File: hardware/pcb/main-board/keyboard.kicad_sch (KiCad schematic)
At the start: 24 parts, among them J201 KB Pico Test Points, U201 KB Pico, U202 Unused 555

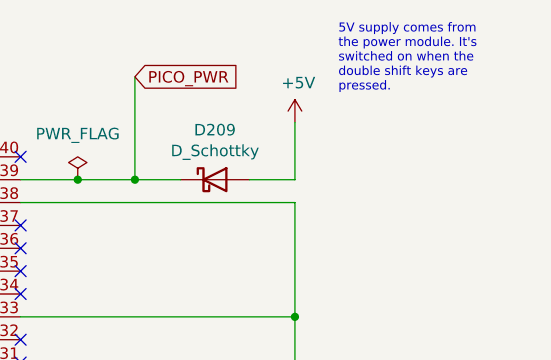
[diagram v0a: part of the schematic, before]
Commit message: start next board iteration, add latch and pico power bits
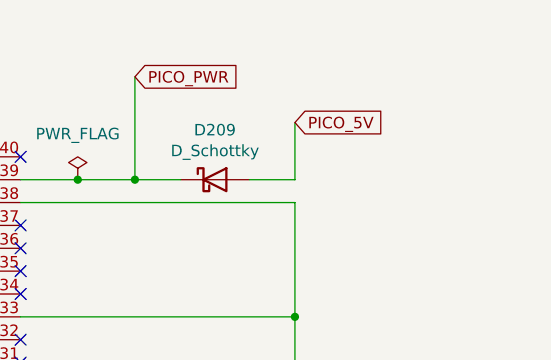
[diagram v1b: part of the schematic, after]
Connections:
- net +5V renamed PICO_5V
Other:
- note removed: "5V supply comes from the power module. It's switched on when the double shift keys are pressed."
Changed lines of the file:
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@@
 	(title_block
 		(title "Z88R - Z88 Recreated")
-		(date "2024-08-23")
-		(rev "20240823")
+		(date "2025-12-19")
+		(rev "20251219WIP")
 		(company "Fountain and Menadue")
 	)
@@
 		)
 	)
-	(text "5V supply comes from\nthe power module. It's\nswitched on when the\ndouble shift keys are\npressed."
-		(exclude_from_sim no)
-		(at 258.826 19.558 0)
-		(effects
-			(font
-				(size 1 1)
-			)
-			(justify left)
-		)
-	)
 	(text "Footprint for a 555, which was originally planned\nto wake the keyboard Pico every 10ms or so. The\nidea was dropped, but it might still be useful.\nNot sure where the 555's power will come from\nthough - the cell battery, like the RTC probably,\nbut it depends how we use it."
 		(exclude_from_sim no)
@@
 		)
 	)
+	(global_label "PICO_5V"
+		(shape input)
+		(at 254 26.67 0)
+		(fields_autoplaced yes)
+		(effects
+			(font
+				(size 1.27 1.27)
+			)
+			(justify left)
+		)
+		(property "Intersheetrefs" "${INTERSHEET_REFS}"
+			(at 264.072 26.67 0)
+			(effects
+				(font
+					(size 1.27 1.27)
+				)
+				(justify left)
+				(hide yes)
+			)
+		)
+	)
 	(global_label "KB_A14"
 		(shape input)
@@
 		(shape output)
 		(at 227.33 63.5 0)
-		(fields_autoplaced yes)
 		(effects
 			(font
@@
 		(shape output)
 		(at 227.33 71.12 0)
-		(fields_autoplaced yes)
 		(effects
 			(font
@@
 					(unit 1)
 				)
-			)
-		)
-	)
-	(symbol
-		(lib_id "power:+5V")
-		(at 254 26.67 0)
-		(unit 1)
-		(exclude_from_sim no)
-		(in_bom yes)
-		(on_board yes)
-		(dnp no)
-		(property "Reference" "#PWR0202"
-			(at 254 30.48 0)
-			(effects
-				(font
-					(size 1.27 1.27)
-				)
-				(hide yes)
-			)
-		)
-		(property "Value" "+5V"
-			(at 254.381 22.2758 0)
-			(effects
-				(font
-					(size 1.27 1.27)
-				)
-			)
-		)
-		(property "Footprint" ""
-			(at 254 26.67 0)
-			(effects
-				(font
-					(size 1.27 1.27)
-				)
-				(hide yes)
-			)
-		)
-		(property "Datasheet" ""
-			(at 254 26.67 0)
-			(effects
-				(font
-					(size 1.27 1.27)
-				)
-				(hide yes)
-			)
-		)
-		(property "Description" "Power symbol creates a global label with name \"+5V\""
-			(at 254 26.67 0)
-			(effects
-				(font
-					(size 1.27 1.27)
-				)
-				(hide yes)
-			)
-		)
-		(pin "1"
-		)
-		(instances
-			(project "z88_new"
-				(path "/fdce8012-5f35-4f58-8abb-80214b4af8fe/611ade0a-1c77-478f-8f5a-a9824ea3de3f"
-					(reference "#PWR0202")
-					(unit 1)
-				)

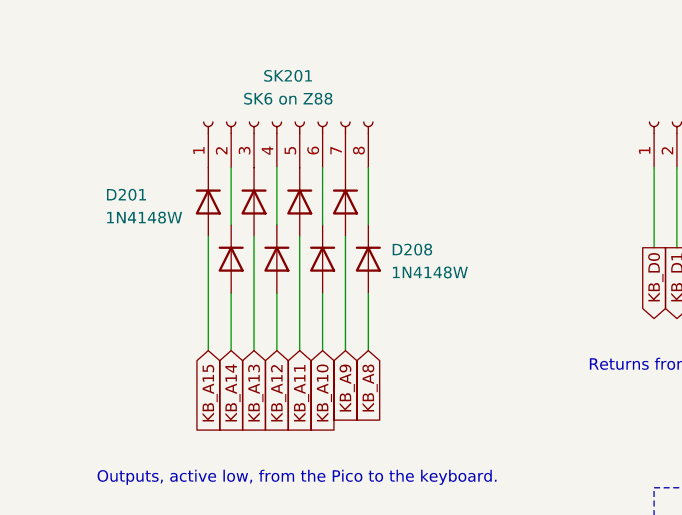
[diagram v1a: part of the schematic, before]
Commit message: turn the KB diodes round, oops
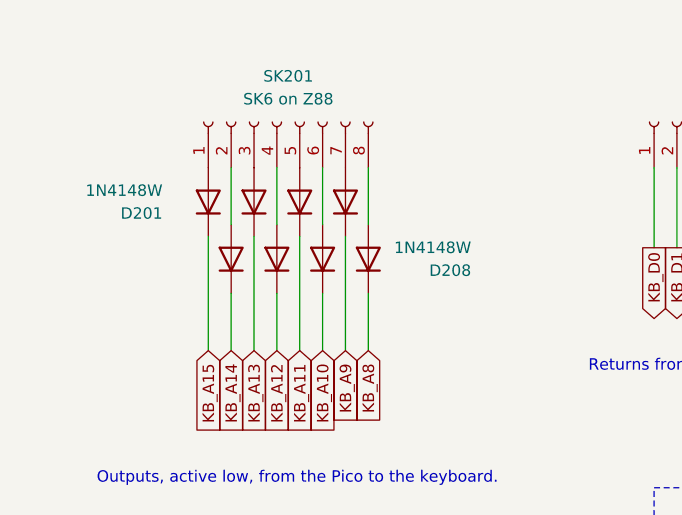
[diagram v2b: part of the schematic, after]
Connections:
- net KB_A10: now also D206.1 (K); no longer D206.2 (A)
- net KB_A11: now also D205.1 (K); no longer D205.2 (A)
- net KB_A12: now also D204.1 (K); no longer D204.2 (A)
- net KB_A13: now also D203.1 (K); no longer D203.2 (A)
- net KB_A14: now also D202.1 (K); no longer D202.2 (A)
- net KB_A15: now also D201.1 (K); no longer D201.2 (A)
- net KB_A8: now also D208.1 (K); no longer D208.2 (A)
- net KB_A9: now also D207.1 (K); no longer D207.2 (A)
- net at SK201.1 (Pin_1): now also D201.2 (A); no longer D201.1 (K)
- net at SK201.2 (Pin_2): now also D202.2 (A); no longer D202.1 (K)
- net at SK201.3 (Pin_3): now also D203.2 (A); no longer D203.1 (K)
- net at SK201.4 (Pin_4): now also D204.2 (A); no longer D204.1 (K)
- net at SK201.5 (Pin_5): now also D205.2 (A); no longer D205.1 (K)
- net at SK201.6 (Pin_6): now also D206.2 (A); no longer D206.1 (K)
- net at SK201.7 (Pin_7): now also D207.2 (A); no longer D207.1 (K)
- net at SK201.8 (Pin_8): now also D208.2 (A); no longer D208.1 (K)
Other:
- moved on the sheet: D201, D208
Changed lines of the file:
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@@
 	(symbol
 		(lib_id "Diode:1N4148W")
-		(at 38.1 40.64 270)
+		(at 38.1 40.64 90)
 		(unit 1)
 		(exclude_from_sim no)
@@
 		(dnp no)
 		(property "Reference" "D203"
-			(at 26.67 39.878 90)
+			(at 49.53 41.402 90)
 			(effects
 				(font
@@
 		)
 		(property "Value" "1N4148W"
-			(at 26.67 42.418 90)
+			(at 49.53 38.862 90)
 			(effects
 				(font
@@
 		)
 		(property "Footprint" "Diode_SMD:D_SOD-123"
-			(at 33.655 40.64 0)
+			(at 42.545 40.64 0)
 			(effects
 				(font
@@
 	(symbol
 		(lib_id "Diode:1N4148W")
-		(at 48.26 40.64 270)
+		(at 48.26 40.64 90)
 		(unit 1)
 		(exclude_from_sim no)
@@
 		(dnp no)
 		(property "Reference" "D207"
-			(at 36.83 39.878 90)
+			(at 59.69 41.402 90)
 			(effects
 				(font
@@
 		)
 		(property "Value" "1N4148W"
-			(at 36.83 42.418 90)
+			(at 59.69 38.862 90)
 			(effects
 				(font
@@
 		)
 		(property "Footprint" "Diode_SMD:D_SOD-123"
-			(at 43.815 40.64 0)
+			(at 52.705 40.64 0)
 			(effects
 				(font
@@
 	(symbol
 		(lib_id "Diode:1N4148W")
-		(at 35.56 46.99 270)
+		(at 35.56 46.99 90)
 		(unit 1)
 		(exclude_from_sim no)
@@
 		(dnp no)
 		(property "Reference" "D202"
-			(at 24.13 46.228 90)
+			(at 46.99 47.752 90)
 			(effects
 				(font
@@
 		)
 		(property "Value" "1N4148W"
-			(at 24.13 48.768 90)
+			(at 46.99 45.212 90)
 			(effects
 				(font
@@
 		)
 		(property "Footprint" "Diode_SMD:D_SOD-123"
-			(at 31.115 46.99 0)
+			(at 40.005 46.99 0)
 			(effects
 				(font
@@
 	(symbol
 		(lib_id "Diode:1N4148W")
-		(at 40.64 46.99 270)
+		(at 40.64 46.99 90)
 		(unit 1)
 		(exclude_from_sim no)
@@
 		(dnp no)
 		(property "Reference" "D204"
-			(at 29.21 46.228 90)
+			(at 52.07 47.752 90)
 			(effects
 				(font
@@
 		)
 		(property "Value" "1N4148W"
-			(at 29.21 48.768 90)
+			(at 52.07 45.212 90)
 			(effects
 				(font
@@
 		)
 		(property "Footprint" "Diode_SMD:D_SOD-123"
-			(at 36.195 46.99 0)
+			(at 45.085 46.99 0)
 			(effects
 				(font
@@
 	(symbol
 		(lib_id "Diode:1N4148W")
-		(at 43.18 40.64 270)
+		(at 43.18 40.64 90)
 		(unit 1)
 		(exclude_from_sim no)
@@
 		(dnp no)
 		(property "Reference" "D205"
-			(at 31.75 39.878 90)
+			(at 54.61 41.402 90)
 			(effects
 				(font
@@
 		)
 		(property "Value" "1N4148W"
-			(at 31.75 42.418 90)
+			(at 54.61 38.862 90)
 			(effects
 				(font
@@
 		)
 		(property "Footprint" "Diode_SMD:D_SOD-123"
-			(at 38.735 40.64 0)
+			(at 47.625 40.64 0)
 			(effects
 				(font
@@
 	(symbol
 		(lib_id "Diode:1N4148W")
-		(at 45.72 46.99 270)
+		(at 45.72 46.99 90)
 		(unit 1)
 		(exclude_from_sim no)
@@
 		(dnp no)
 		(property "Reference" "D206"
-			(at 34.29 46.228 90)
+			(at 57.15 47.752 90)
 			(effects
 				(font
@@
 		)
 		(property "Value" "1N4148W"
-			(at 34.29 48.768 90)
+			(at 57.15 45.212 90)
 			(effects
 				(font
@@
 		)
 		(property "Footprint" "Diode_SMD:D_SOD-123"
-			(at 41.275 46.99 0)
+			(at 50.165 46.99 0)
 			(effects
 				(font
@@
 	(symbol
 		(lib_id "Diode:1N4148W")
-		(at 33.02 40.64 270)
+		(at 33.02 40.64 90)
 		(unit 1)
 		(exclude_from_sim no)
@@
 		(dnp no)
 		(property "Reference" "D201"
-			(at 21.59 39.878 90)
+			(at 27.94 41.91 90)
 			(effects
 				(font
@@
 		)
 		(property "Value" "1N4148W"
-			(at 21.59 42.418 90)
+			(at 27.94 39.37 90)
 			(effects
 				(font
@@
 		)
 		(property "Footprint" "Diode_SMD:D_SOD-123"
-			(at 28.575 40.64 0)
+			(at 37.465 40.64 0)
 			(effects
 				(font
@@
 	(symbol
 		(lib_id "Diode:1N4148W")
-		(at 50.8 46.99 270)
+		(at 50.8 46.99 90)
 		(unit 1)
 		(exclude_from_sim no)
@@
 		(dnp no)
 		(property "Reference" "D208"
-			(at 53.34 45.974 90)
+			(at 62.23 48.26 90)
 			(effects
 				(font
@@
 		)
 		(property "Value" "1N4148W"
-			(at 53.34 48.514 90)
+			(at 62.23 45.72 90)
 			(effects
 				(font
@@
 		)
 		(property "Footprint" "Diode_SMD:D_SOD-123"
-			(at 46.355 46.99 0)
-			(effects
-				(font
+			(at 55.245 46.99 0)
+			(effects
+				(font

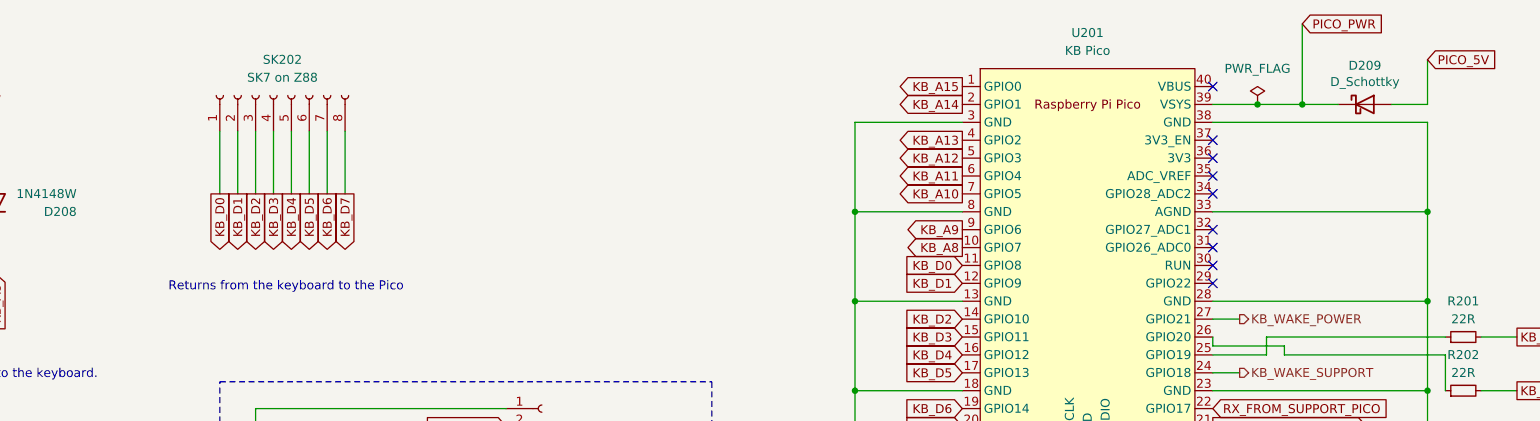
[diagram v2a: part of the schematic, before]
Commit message: make a start on RP2040 to replace the KB pico
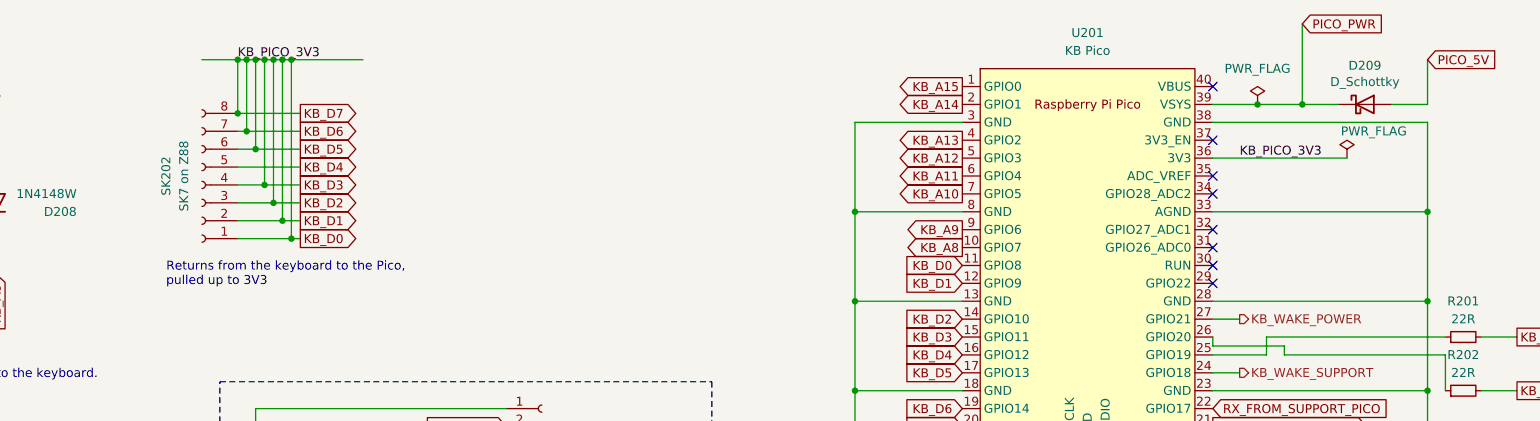
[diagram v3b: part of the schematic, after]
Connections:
- net KB_D1 is gone; now on net KB_D0: SK202.2 (Pin_2), U201.12 (GPIO9)
- net KB_D2 is gone; now on net KB_D0: SK202.3 (Pin_3), U201.14 (GPIO10)
- net KB_D3 is gone; now on net KB_D0: SK202.4 (Pin_4), U201.15 (GPIO11)
- net KB_D5 is gone; now on net KB_D0: SK202.6 (Pin_6), U201.17 (GPIO13)
- net KB_D6 is gone; now on net KB_D0: SK202.7 (Pin_7), U201.19 (GPIO14)
- net KB_D7 is gone; now on net KB_D0: SK202.8 (Pin_8), U201.20 (GPIO15)
- net KB_D0: now also U201.36 (3V3)
- no-connect marks 10 -> 9
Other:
- note added: "Returns from the keyboard to the Pico, pulled up to 3V3"
- note removed: "Returns from the keyboard to the Pico"
- title: Z88R - Z88 Recreated -> Z88R - Z88 Recreation
- moved on the sheet: SK202

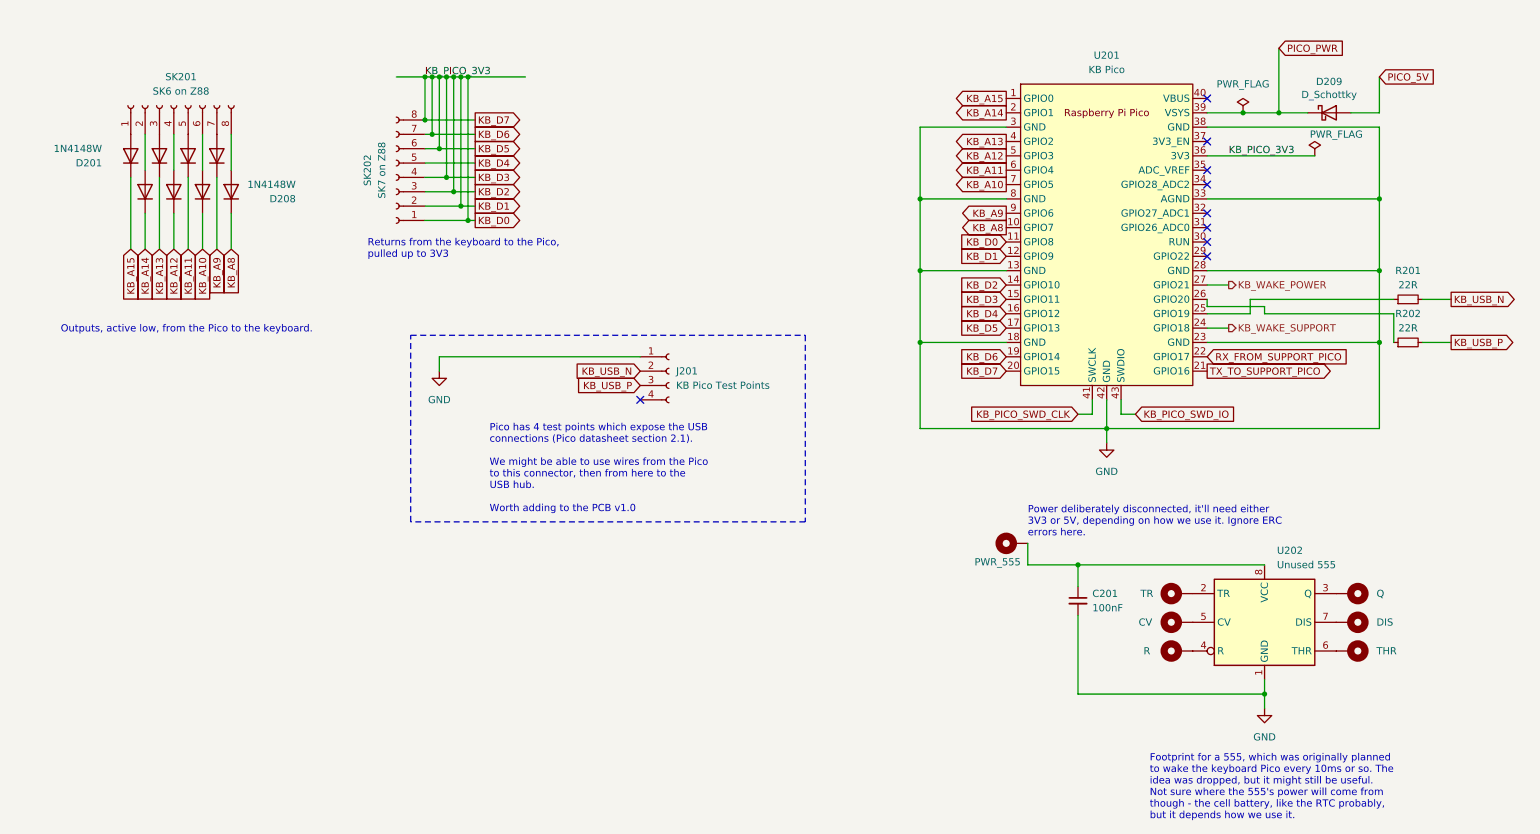
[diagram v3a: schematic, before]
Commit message: more working out of the KB pico replacement
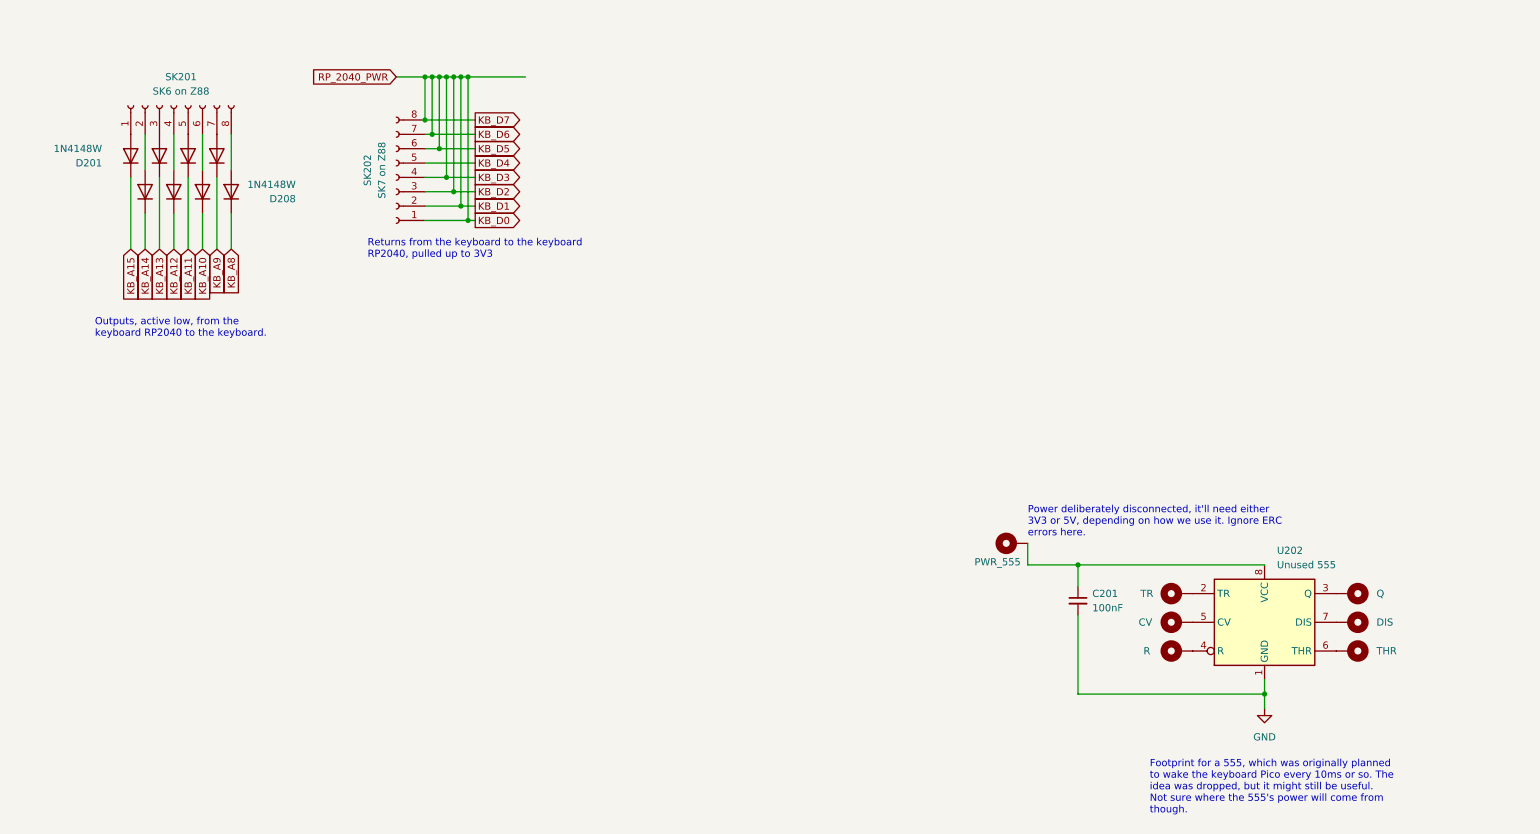
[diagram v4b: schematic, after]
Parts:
- removed D209: D_Schottky, Diode_SMD:D_1206_3216Metric_Pad1.42x1.75mm_HandSolder, symbol Device:D_Schottky
- removed J201: KB Pico Test Points, Connector_PinHeader_1.00mm:PinHeader_1x04_P1.00mm_Vertical, symbol Connector:Conn_01x04_Socket
- removed R201, R202: 22R, Resistor_SMD:R_0805_2012Metric_Pad1.20x1.40mm_HandSolder, symbol Device:R_Small
- removed U201: KB Pico, Pico:RPi_Pico_SMD_TH, symbol RP Pico:Pico
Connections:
- no-connect marks 9 -> 0
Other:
- note added: "Footprint for a 555, which was originally planned to wake the keyboard Pico every 10ms or so. The idea was dropped, but it might still be useful. Not sure where the 555's power will come from though."
- note added: "Outputs, active low, from the keyboard RP2040 to the keyboard."
- note added: "Returns from the keyboard to the keyboard RP2040, pulled up to 3V3"
- note removed: "Footprint for a 555, which was originally planned to wake the keyboard Pico every 10ms or so. The idea was dropped, but it might still be useful. Not sure where the 555's power will come from though - the cell battery, like the RTC probably, but it depends how we use it."
- note removed: "Outputs, active low, from the Pico to the keyboard."
- note removed: "Pico has 4 test points which expose the USB connections (Pico datasheet section 2.1). We might be able to use wires from the Pico to this connector, then from here to the USB hub. Worth adding to the PCB v1.0"
- note removed: "Returns from the keyboard to the Pico, pulled up to 3V3"
